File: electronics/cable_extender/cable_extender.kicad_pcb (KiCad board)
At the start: 2 copper layers, 2 parts

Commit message: trying out the pitch and matching of the hole grids
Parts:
- added J1: Conn_01x11, SquantorConnectors:hole_row-0254-1X11-H010-ELONG, F.Cu at (160.0, 66.0)
- added J2: Conn_01x06, SquantorConnectors:hole_row-0508-1X06-H015-ELONG, F.Cu at (160.0, 71.1)
- added J3: Conn_01x06, SquantorConnectors:hole_row-0508-1X06-H015-ELONG, F.Cu at (160.0, 83.8)
- added J4: Conn_01x11, SquantorConnectors:hole_row-0254-1X11-H010-ELONG, F.Cu at (160.0, 88.9)
- N1: value 20200610 -> 20200615
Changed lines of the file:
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@@
     (tracks 0)
     (zones 0)
-    (modules 2)
-    (nets 1)
+    (modules 6)
+    (nets 12)
   )
   (page A4)
@@
   )
   (net 0 "")
+  (net 1 /PIN_11)
+  (net 2 /PIN_10)
+  (net 3 /PIN_09)
+  (net 4 /PIN_08)
+  (net 5 /PIN_07)
+  (net 6 /PIN_06)
+  (net 7 /PIN_05)
+  (net 8 /PIN_04)
+  (net 9 /PIN_03)
+  (net 10 /PIN_02)
+  (net 11 /PIN_01)
   (net_class Default "This is the default net class."
     (clearance 0.2)
@@
     (uvia_dia 0.3)
     (uvia_drill 0.1)
+    (add_net /PIN_01)
+    (add_net /PIN_02)
+    (add_net /PIN_03)
+    (add_net /PIN_04)
+    (add_net /PIN_05)
+    (add_net /PIN_06)
+    (add_net /PIN_07)
+    (add_net /PIN_08)
+    (add_net /PIN_09)
+    (add_net /PIN_10)
+    (add_net /PIN_11)
+  )
+  (module SquantorConnectors:hole_row-0254-1X11-H010-ELONG (layer F.Cu)
+    (at 160.02 88.9)
+    (fp_text reference J4 (at 0 -3.81) (layer F.SilkS)
+      (effects (font (size 1 1) (thickness 0.15)))
+    )
+    (fp_text value Conn_01x11 (at 0 3.81) (layer F.Fab)
+      (effects (font (size 1 1) (thickness 0.15)))
+    )
+    (pad 11 thru_hole oval (at 12.7 0) (size 1.5 3) (drill 1) (layers *.Cu *.Mask)
+      (net 1 /PIN_11))
+    (pad 10 thru_hole oval (at 10.16 0) (size 1.5 3) (drill 1) (layers *.Cu *.Mask)
+      (net 2 /PIN_10))
+    (pad 9 thru_hole oval (at 7.62 0) (size 1.5 3) (drill 1) (layers *.Cu *.Mask)
+      (net 3 /PIN_09))
+    (pad 8 thru_hole oval (at 5.08 0) (size 1.5 3) (drill 1) (layers *.Cu *.Mask)
+      (net 4 /PIN_08))
+    (pad 7 thru_hole oval (at 2.54 0) (size 1.5 3) (drill 1) (layers *.Cu *.Mask)
+      (net 5 /PIN_07))
+    (pad 6 thru_hole oval (at 0 0) (size 1.5 3) (drill 1) (layers *.Cu *.Mask)
+      (net 6 /PIN_06))
+    (pad 5 thru_hole oval (at -2.54 0) (size 1.5 3) (drill 1) (layers *.Cu *.Mask)
+      (net 7 /PIN_05))
+    (pad 4 thru_hole oval (at -5.08 0) (size 1.5 3) (drill 1) (layers *.Cu *.Mask)
+      (net 8 /PIN_04))
+    (pad 3 thru_hole oval (at -7.62 0) (size 1.5 3) (drill 1) (layers *.Cu *.Mask)
+      (net 9 /PIN_03))
+    (pad 2 thru_hole oval (at -10.16 0) (size 1.5 3) (drill 1) (layers *.Cu *.Mask)
+      (net 10 /PIN_02))
+    (pad 1 thru_hole roundrect (at -12.7 0) (size 1.5 3) (drill 1) (layers *.Cu *.Mask) (roundrect_rratio 0.25)
+      (net 11 /PIN_01))
+  )
+  (module SquantorConnectors:hole_row-0508-1X06-H015-ELONG (layer F.Cu)
+    (at 160.02 83.82)
+    (tags "generic hole row")
+    (fp_text reference J3 (at 0 -3.81) (layer F.SilkS)
+      (effects (font (size 1 1) (thickness 0.15)))
+    )
+    (fp_text value Conn_01x06 (at 0 3.81) (layer F.Fab)
+      (effects (font (size 1 1) (thickness 0.15)))
+    )
+    (pad 6 thru_hole oval (at 12.7 0) (size 2 4) (drill 1.5) (layers *.Cu *.Mask)
+      (net 1 /PIN_11))
+    (pad 5 thru_hole oval (at 7.62 0) (size 2 4) (drill 1.5) (layers *.Cu *.Mask)
+      (net 3 /PIN_09))
+    (pad 4 thru_hole oval (at 2.54 0) (size 2 4) (drill 1.5) (layers *.Cu *.Mask)
+      (net 5 /PIN_07))
+    (pad 3 thru_hole oval (at -2.54 0) (size 2 4) (drill 1.5) (layers *.Cu *.Mask)
+      (net 7 /PIN_05))
+    (pad 2 thru_hole oval (at -7.62 0) (size 2 4) (drill 1.5) (layers *.Cu *.Mask)
+      (net 9 /PIN_03))
+    (pad 1 thru_hole roundrect (at -12.7 0) (size 2 4) (drill 1.5) (layers *.Cu *.Mask) (roundrect_rratio 0.25)
+      (net 11 /PIN_01))
+  )
+  (module SquantorConnectors:hole_row-0508-1X06-H015-ELONG (layer F.Cu)
+    (at 160.02 71.12)
+    (tags "generic hole row")
+    (fp_text reference J2 (at 0 -3.81) (layer F.SilkS)
+      (effects (font (size 1 1) (thickness 0.15)))
+    )
+    (fp_text value Conn_01x06 (at 0 3.81) (layer F.Fab)
+      (effects (font (size 1 1) (thickness 0.15)))
+    )
+    (pad 6 thru_hole oval (at 12.7 0) (size 2 4) (drill 1.5) (layers *.Cu *.Mask)
+      (net 1 /PIN_11))
+    (pad 5 thru_hole oval (at 7.62 0) (size 2 4) (drill 1.5) (layers *.Cu *.Mask)
+      (net 3 /PIN_09))
+    (pad 4 thru_hole oval (at 2.54 0) (size 2 4) (drill 1.5) (layers *.Cu *.Mask)
+      (net 5 /PIN_07))
+    (pad 3 thru_hole oval (at -2.54 0) (size 2 4) (drill 1.5) (layers *.Cu *.Mask)
+      (net 7 /PIN_05))
+    (pad 2 thru_hole oval (at -7.62 0) (size 2 4) (drill 1.5) (layers *.Cu *.Mask)
+      (net 9 /PIN_03))
+    (pad 1 thru_hole roundrect (at -12.7 0) (size 2 4) (drill 1.5) (layers *.Cu *.Mask) (roundrect_rratio 0.25)
+      (net 11 /PIN_01))
+  )
+  (module SquantorConnectors:hole_row-0254-1X11-H010-ELONG (layer F.Cu)
+    (at 160.02 66.04)
+    (fp_text reference J1 (at 0 -3.81) (layer F.SilkS)
+      (effects (font (size 1 1) (thickness 0.15)))
+    )
+    (fp_text value Conn_01x11 (at 0 3.81) (layer F.Fab)
+      (effects (font (size 1 1) (thickness 0.15)))
+    )
+    (pad 11 thru_hole oval (at 12.7 0) (size 1.5 3) (drill 1) (layers *.Cu *.Mask)
+      (net 1 /PIN_11))
+    (pad 10 thru_hole oval (at 10.16 0) (size 1.5 3) (drill 1) (layers *.Cu *.Mask)
+      (net 2 /PIN_10))
+    (pad 9 thru_hole oval (at 7.62 0) (size 1.5 3) (drill 1) (layers *.Cu *.Mask)
+      (net 3 /PIN_09))
+    (pad 8 thru_hole oval (at 5.08 0) (size 1.5 3) (drill 1) (layers *.Cu *.Mask)
+      (net 4 /PIN_08))
+    (pad 7 thru_hole oval (at 2.54 0) (size 1.5 3) (drill 1) (layers *.Cu *.Mask)
+      (net 5 /PIN_07))
+    (pad 6 thru_hole oval (at 0 0) (size 1.5 3) (drill 1) (layers *.Cu *.Mask)
+      (net 6 /PIN_06))
+    (pad 5 thru_hole oval (at -2.54 0) (size 1.5 3) (drill 1) (layers *.Cu *.Mask)
+      (net 7 /PIN_05))
+    (pad 4 thru_hole oval (at -5.08 0) (size 1.5 3) (drill 1) (layers *.Cu *.Mask)
+      (net 8 /PIN_04))
+    (pad 3 thru_hole oval (at -7.62 0) (size 1.5 3) (drill 1) (layers *.Cu *.Mask)
+      (net 9 /PIN_03))
+    (pad 2 thru_hole oval (at -10.16 0) (size 1.5 3) (drill 1) (layers *.Cu *.Mask)
+      (net 10 /PIN_02))
+    (pad 1 thru_hole roundrect (at -12.7 0) (size 1.5 3) (drill 1) (layers *.Cu *.Mask) (roundrect_rratio 0.25)
+      (net 11 /PIN_01))
   )
   (module Symbol:OSHW-Symbol_6.7x6mm_SilkScreen (layer F.Cu)
@@
       (effects (font (size 1 1) (thickness 0.15)))
     )
-    (fp_text value 20200610 (at 0.8 -0.1) (layer F.SilkS)
+    (fp_text value 20200615 (at 0.8 -0.1) (layer F.SilkS)
       (effects (font (size 0.8 0.8) (thickness 0.15)))
     )

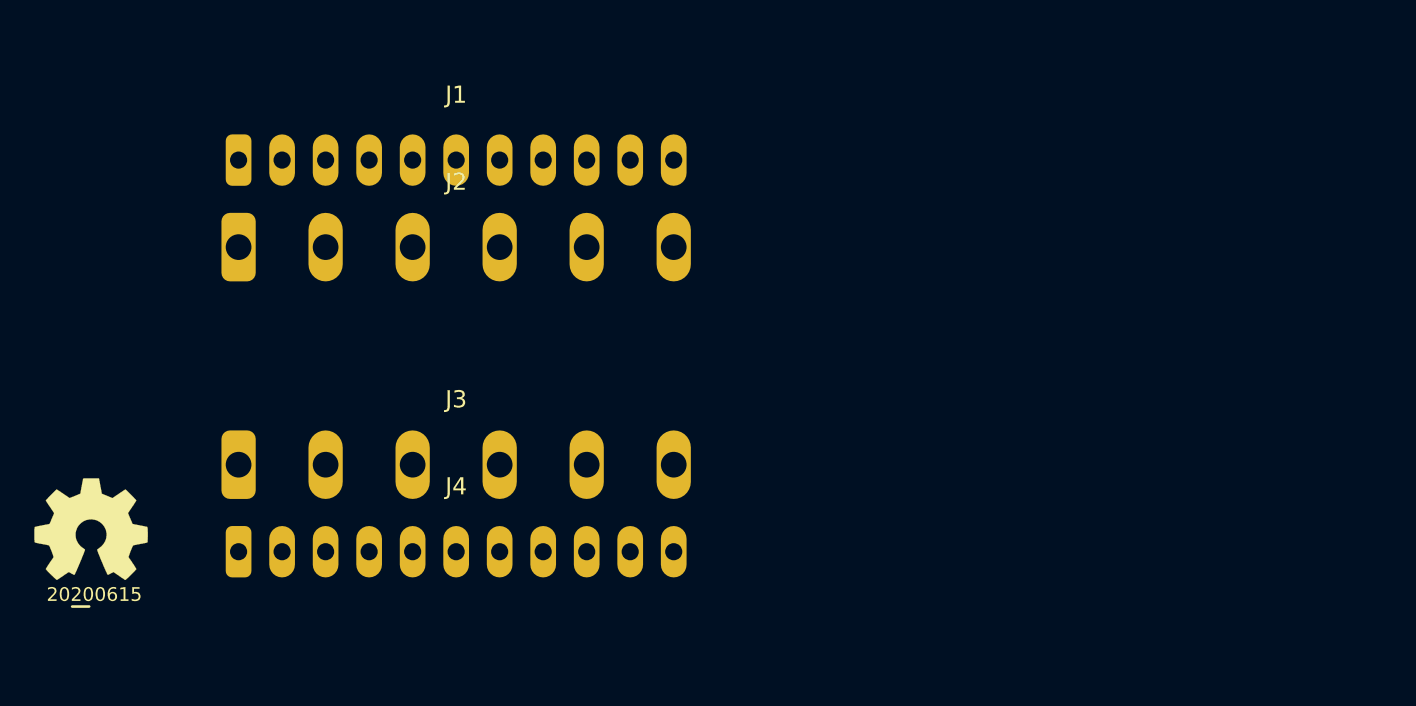
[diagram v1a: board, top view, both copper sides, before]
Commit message: added more hole rows
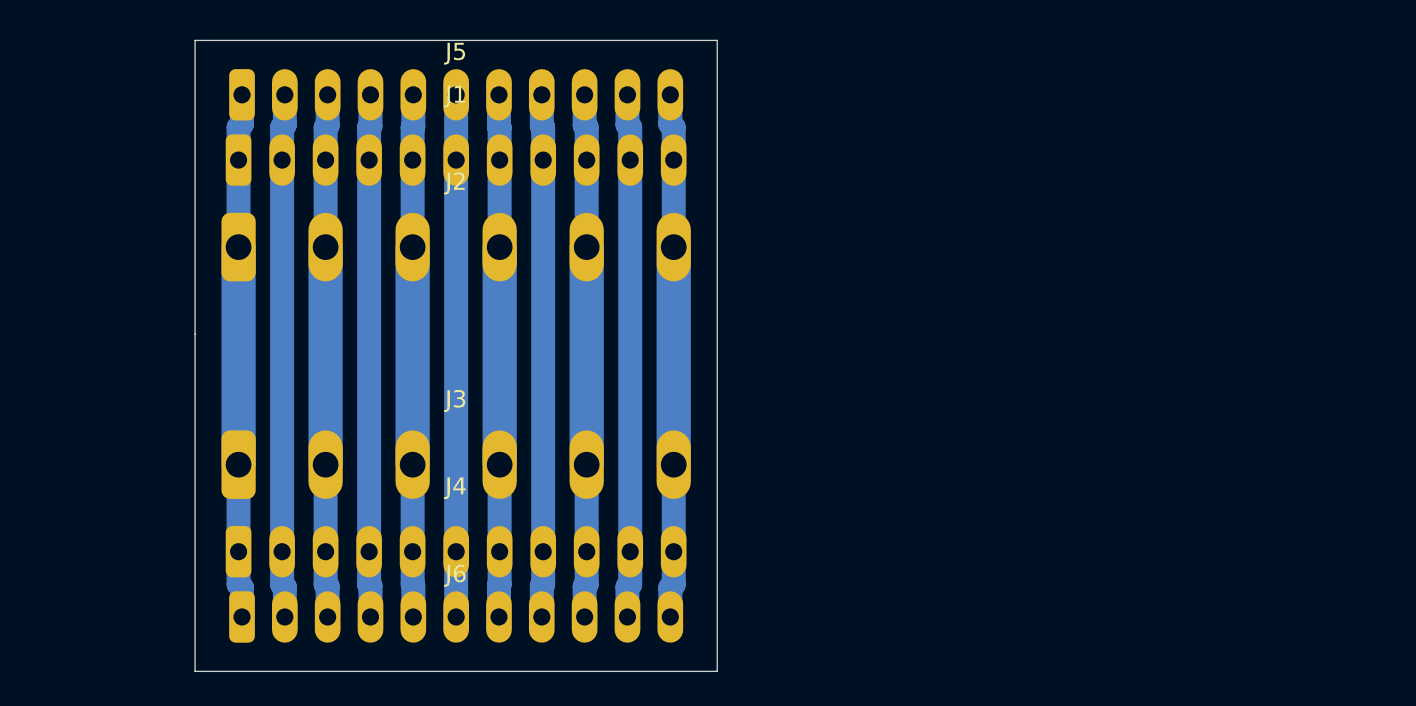
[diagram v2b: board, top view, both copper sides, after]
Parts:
- added J5: Conn_01x11, SquantorConnectors:hole_row-0250-1X11-H010-ELONG, F.Cu at (160.0, 62.2)
- added J6: Conn_01x11, SquantorConnectors:hole_row-0250-1X11-H010-ELONG, F.Cu at (160.0, 92.7)
- N1, N2: moved to B.Cu
- moved N1 24.7 mm to (160.3, 80.7), turned to 180 degrees
- moved N2 23.7 mm to (159.8, 76.8), turned to 180 degrees
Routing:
- net /PIN_01: track 0.00 -> 30.6 mm
- net /PIN_11: track 0.00 -> 30.6 mm
- net /PIN_10: track 0.00 -> 30.6 mm
- net /PIN_02: track 0.00 -> 30.6 mm
- net /PIN_03: track 0.00 -> 30.6 mm
- net /PIN_09: track 0.00 -> 30.6 mm
- net /PIN_04: track 0.00 -> 30.5 mm
- net /PIN_08: track 0.00 -> 30.5 mm
- net /PIN_05: track 0.00 -> 30.5 mm
- net /PIN_07: track 0.00 -> 30.5 mm
- net /PIN_06: track 0.00 -> 30.5 mm
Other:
- board outline added: 30.5 x 36.8 mm

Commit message: rearranged connector positions
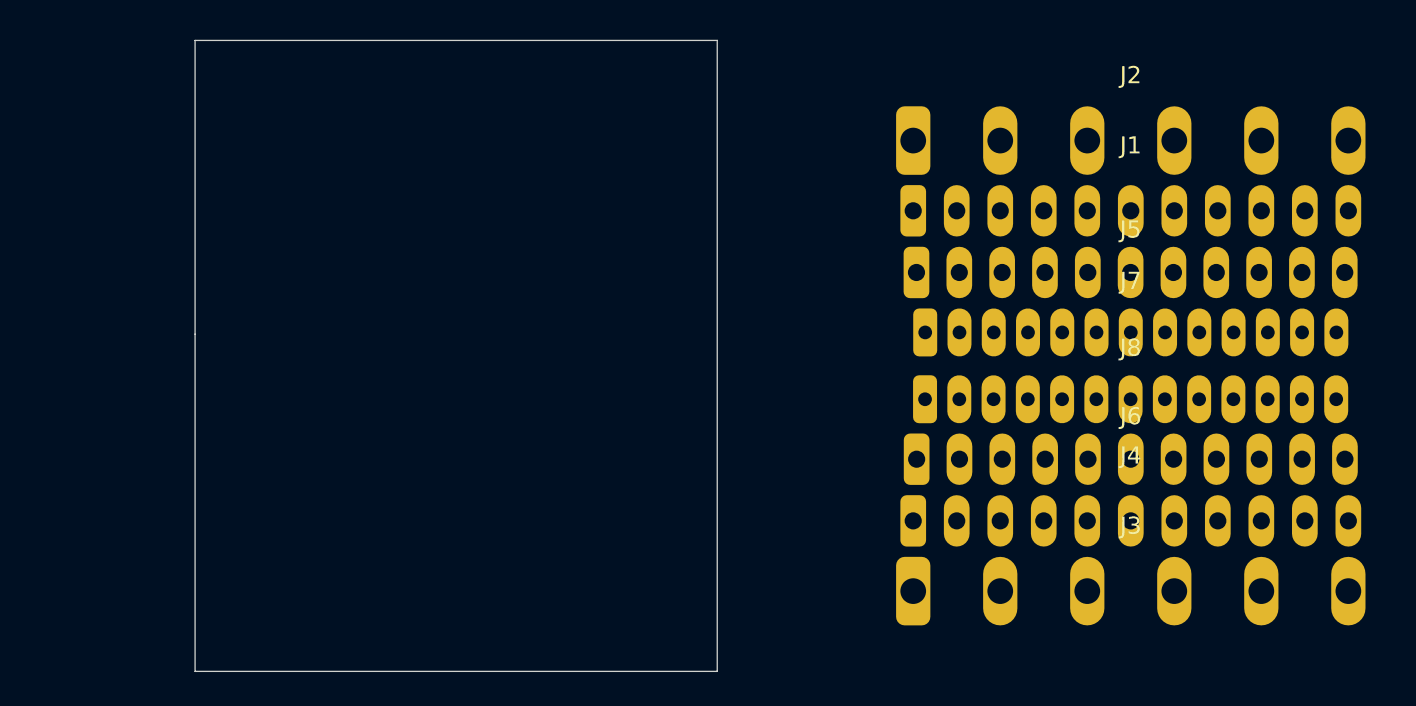
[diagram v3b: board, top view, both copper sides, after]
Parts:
- added J7: Conn_01x13, SquantorConnectors:hole_row-0200-1X13-H008-ELONG, F.Cu at (199.4, 76.1)
- added J8: Conn_01x13, SquantorConnectors:hole_row-0200-1X13-H008-ELONG, F.Cu at (199.4, 80.0)
- moved J5 40.7 mm to (199.4, 72.6)
- moved J6 40.4 mm to (199.4, 83.5)
- moved J3 40.1 mm to (199.4, 91.2)
- moved J2 39.9 mm to (199.4, 64.9)
- moved J1 39.5 mm to (199.4, 69.0)
- moved J4 39.4 mm to (199.4, 87.1)
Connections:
- net /PIN_10 renamed /PIN_12
- J1 pad 11: /PIN_11 -> /PIN_13
- J1 pad 5: /PIN_05 -> /PIN_06
- J1 pad 6: /PIN_06 -> /PIN_07
- J1 pad 7: /PIN_07 -> /PIN_08
- J1 pad 8: /PIN_08 -> /PIN_09
- J1 pad 9: /PIN_09 -> /PIN_11
- J2 pad 3: /PIN_05 -> /PIN_06
- J2 pad 4: /PIN_07 -> /PIN_08
- J2 pad 5: /PIN_09 -> /PIN_11
- J2 pad 6: /PIN_11 -> /PIN_13
- J3 pad 3: /PIN_05 -> /PIN_06
- J3 pad 4: /PIN_07 -> /PIN_08
- J3 pad 5: /PIN_09 -> /PIN_11
- J3 pad 6: /PIN_11 -> /PIN_13
- J4 pad 11: /PIN_11 -> /PIN_13
- J4 pad 5: /PIN_05 -> /PIN_06
- J4 pad 6: /PIN_06 -> /PIN_07
- J4 pad 7: /PIN_07 -> /PIN_08
- J4 pad 8: /PIN_08 -> /PIN_09
- J4 pad 9: /PIN_09 -> /PIN_11
- J5 pad 11: /PIN_11 -> /PIN_13
- J5 pad 5: /PIN_05 -> /PIN_06
- J5 pad 6: /PIN_06 -> /PIN_07
- J5 pad 7: /PIN_07 -> /PIN_08
- J5 pad 8: /PIN_08 -> /PIN_09
- J5 pad 9: /PIN_09 -> /PIN_11
- J6 pad 11: /PIN_11 -> /PIN_13
- J6 pad 5: /PIN_05 -> /PIN_06
- J6 pad 6: /PIN_06 -> /PIN_07
- J6 pad 7: /PIN_07 -> /PIN_08
- J6 pad 8: /PIN_08 -> /PIN_09
- J6 pad 9: /PIN_09 -> /PIN_11
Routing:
- net /PIN_01: track 30.6 -> 0.00 mm
- net /PIN_11: track 30.6 -> 0.00 mm
- net /PIN_12: track 30.6 -> 0.00 mm
- net /PIN_02: track 30.6 -> 0.00 mm
- net /PIN_03: track 30.6 -> 0.00 mm
- net /PIN_09: track 30.6 -> 0.00 mm
- net /PIN_04: track 30.5 -> 0.00 mm
- net /PIN_08: track 30.5 -> 0.00 mm
- net /PIN_05: track 30.5 -> 0.00 mm
- net /PIN_07: track 30.5 -> 0.00 mm
- net /PIN_06: track 30.5 -> 0.00 mm

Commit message: board outline
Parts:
- moved N1 34.7 mm to (184.6, 105.5)
- moved N2 34.7 mm to (183.9, 101.6)
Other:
- board size 30.5 x 36.8 mm -> 28.8 x 31.7 mm
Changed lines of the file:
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@@
   (general
     (thickness 1.6)
-    (drawings 5)
+    (drawings 4)
     (tracks 0)
     (zones 0)
@@
   )
   (module Symbol:OSHW-Symbol_6.7x6mm_SilkScreen (layer B.Cu)
-    (at 159.75 76.805 180)
+    (at 183.95 101.605 180)
     (descr "Open Source Hardware Symbol")
     (tags "Logo Symbol OSHW")
@@
   )
   (module SquantorLabels:Label_Generic (layer B.Cu)
-    (at 160.35 80.705 180)
+    (at 184.55 105.505 180)
     (descr "Label for general purpose use")
     (tags Label)
@@
     (fp_line (start -0.5 -0.6) (end 0.5 -0.6) (layer B.SilkS) (width 0.15))
   )
-  (gr_line (start 144.78 95.885) (end 144.78 76.2) (layer Edge.Cuts) (width 0.05))
-  (gr_line (start 175.26 95.885) (end 144.78 95.885) (layer Edge.Cuts) (width 0.05))
-  (gr_line (start 175.26 59.055) (end 175.26 95.885) (layer Edge.Cuts) (width 0.05))
-  (gr_line (start 144.78 59.055) (end 175.26 59.055) (layer Edge.Cuts) (width 0.05))
-  (gr_line (start 144.78 76.2) (end 144.78 59.055) (layer Edge.Cuts) (width 0.05))
+  (gr_line (start 185 62.2) (end 185 93.9) (layer Edge.Cuts) (width 0.05))
+  (gr_line (start 213.8 62.2) (end 185 62.2) (layer Edge.Cuts) (width 0.05))
+  (gr_line (start 213.8 93.9) (end 213.8 62.2) (layer Edge.Cuts) (width 0.05))
+  (gr_line (start 185 93.9) (end 213.8 93.9) (layer Edge.Cuts) (width 0.05))
 )

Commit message: routing completed
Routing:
- net /PIN_13: track 0.00 -> 26.9 mm
- net /PIN_01: track 0.00 -> 26.9 mm
- net /PIN_11: track 0.00 -> 26.8 mm
- net /PIN_03: track 0.00 -> 26.8 mm
- net /PIN_08: track 0.00 -> 26.8 mm
- net /PIN_06: track 0.00 -> 26.7 mm
- net /PIN_09: track 0.00 -> 19.0 mm
- net /PIN_04: track 0.00 -> 19.0 mm
- net /PIN_12: track 0.00 -> 18.2 mm
- net /PIN_02: track 0.00 -> 18.2 mm
- net /PIN_07: track 0.00 -> 18.1 mm
- net /PIN_10: track 0.00 -> 3.90 mm
- net /PIN_05: track 0.00 -> 3.90 mm

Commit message: added top groundplane
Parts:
- removed N1: 20200615, SquantorLabels:Label_Generic
- removed N2: OHWLOGO, Symbol:OSHW-Symbol_6.7x6mm_SilkScreen
- added TP1: testpad, SquantorTestPoints:TestPoint_Hole_D0.8mm, F.Cu at (212.9, 78.1)
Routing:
- added copper zone on F.Cu, net GND
